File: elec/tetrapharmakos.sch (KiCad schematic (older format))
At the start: 12 parts

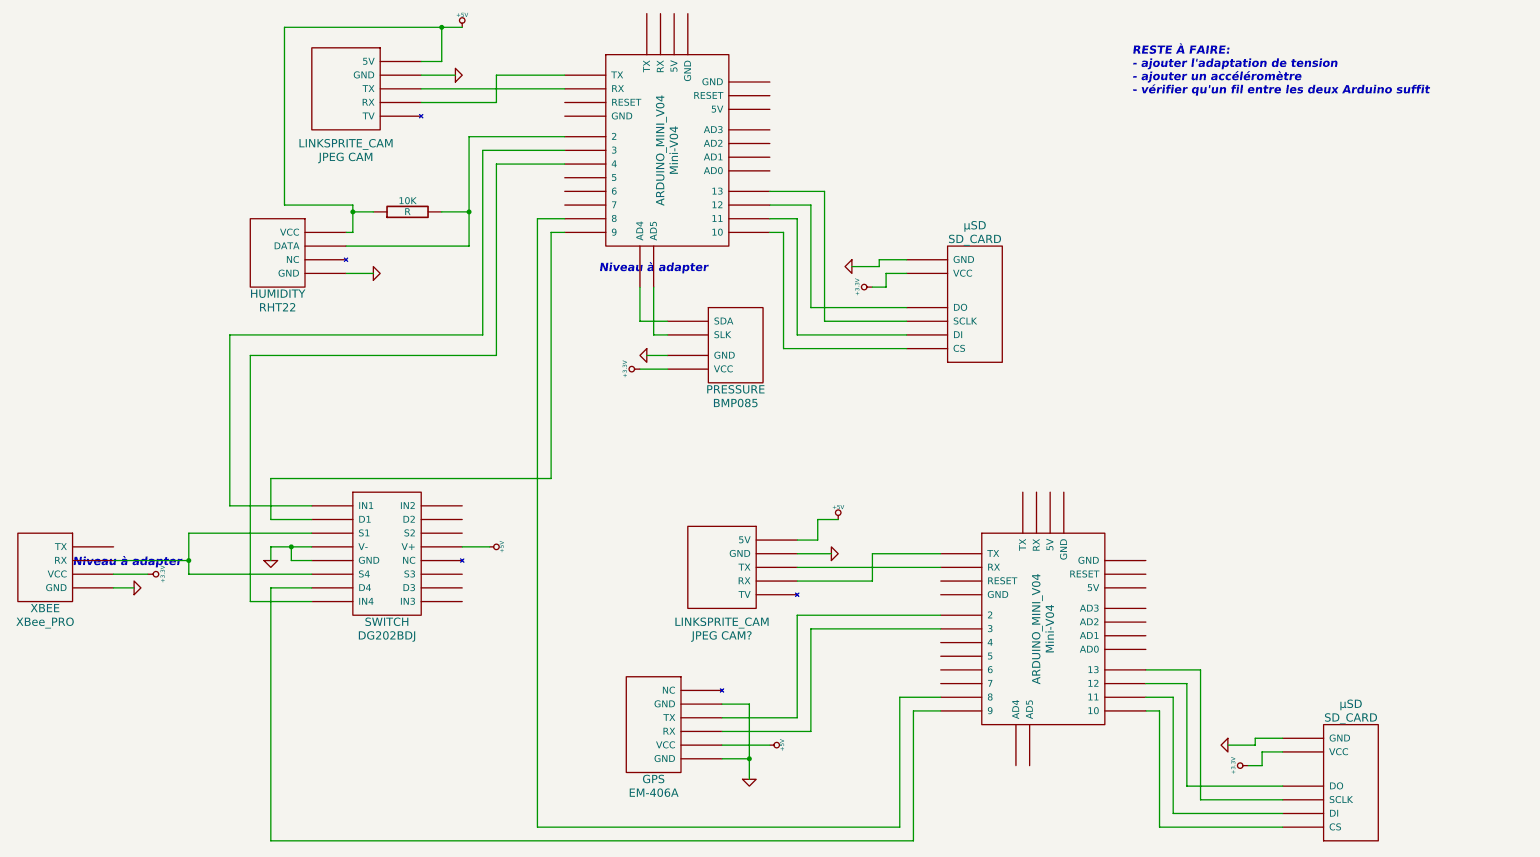
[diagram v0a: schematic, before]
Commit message: Ajout de l'accéléromètre numérique dans le schéma électronique
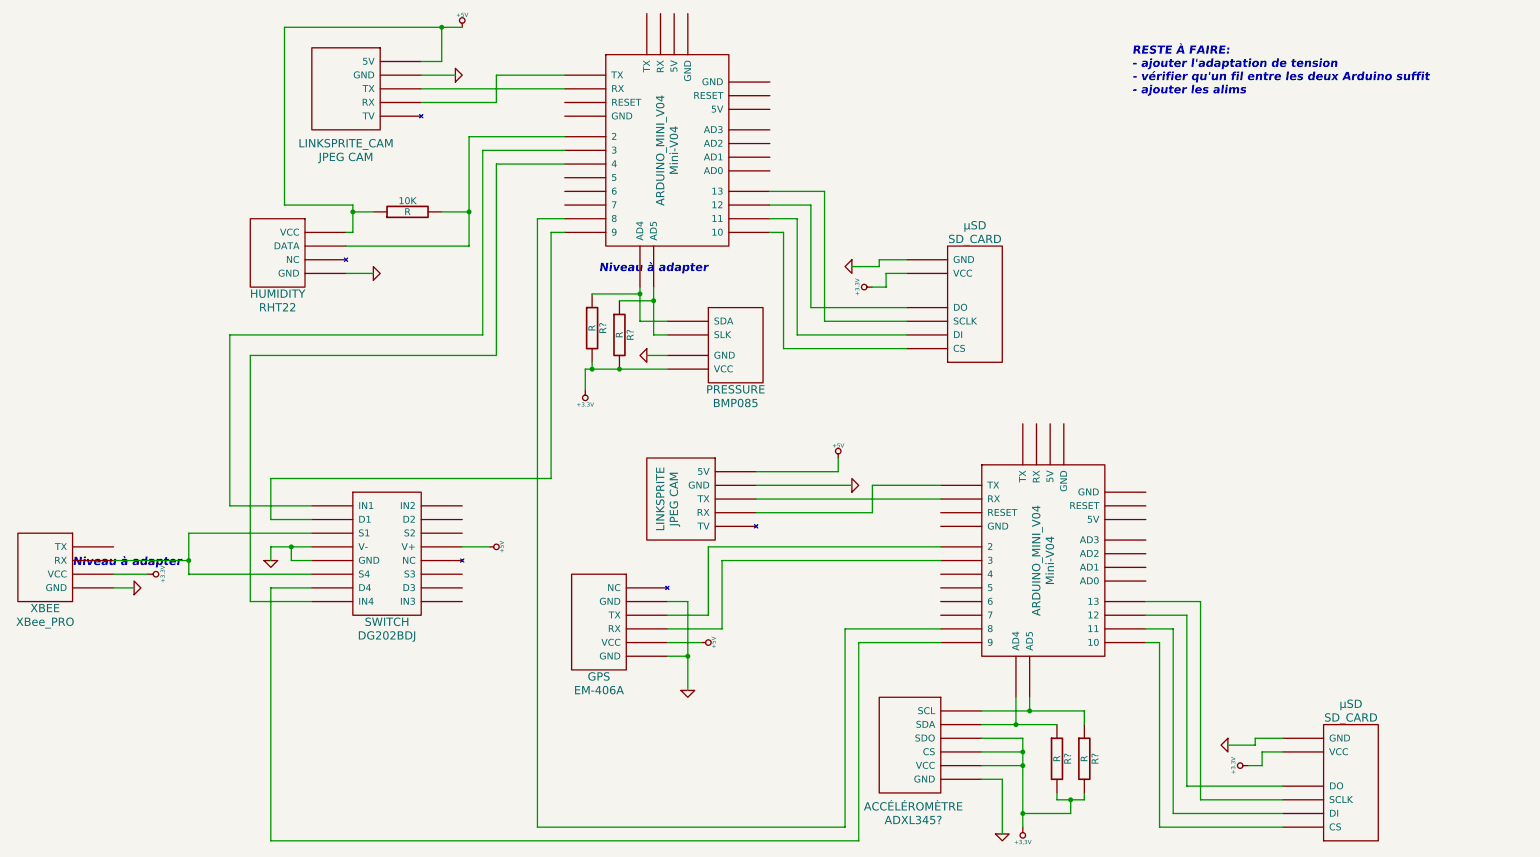
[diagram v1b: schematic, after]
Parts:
- added ADXL345?: ACCÉLÉROMÈTRE, symbol ACCÉLÉROMÈTRE
- added R? (x4): R, symbol R
- JPEG: renamed from JPEG~CAM?; value LINKSPRITE_CAM -> LINKSPRITE
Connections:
- net +3.3V: now also ADXL345?.~ (VCC), R?.2, R?.2, R?.2, R?.2
- net GND: now also ADXL345?.~ (VCC)
- net at Mini-V04.~ (TX): now also DG202BDJ.~ (V-)
- net at Mini-V04.~ (TX): now also ADXL345?.~ (VCC), R?.1; no longer Mini-V04.~ (TX)
- new net: Mini-V04.~ (TX), µSD.~ (VCC) (x8)
- new net: JPEG~CAM.~ (TX), Mini-V04.~ (TX) (x2)
- new net: BMP085.~ (VCC), Mini-V04.~ (TX), R?.1 (x2)
- new net: 10K.2, Mini-V04.~ (TX), RHT22.~ (VCC)
- new net: Mini-V04.~ (TX), Mini-V04.~ (TX)
- new net: DG202BDJ.~ (V-), Mini-V04.~ (TX) (x3)
- new net: JPEG.~ (TX), Mini-V04.~ (TX) (x2)
- new net: EM-406A.~ (VCC), Mini-V04.~ (TX) (x2)
- new net: ADXL345?.~ (VCC), Mini-V04.~ (TX), R?.1
- new net: DG202BDJ.~ (V-), XBee_PRO.~ (VCC)
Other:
- note added: "RESTE À FAIRE:\n- ajouter l'adaptation de tension\n- vérifier qu'un fil entre les deux Arduino suffit\n- ajouter les alims"
- note removed: "RESTE À FAIRE:\n- ajouter l'adaptation de tension\n- ajouter un accéléromètre\n- vérifier qu'un fil entre les deux Arduino suffit"
- moved on the sheet: EM-406A, JPEG CAM, Mini-V04

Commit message: changement des fichiers du programme de l'Arduino n°1 en liens symboliques
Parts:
- renumbered JPEG~CAM to JPEG
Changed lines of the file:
@@
-EESchema Schematic File Version 2  date dim. 29 juil. 2012 12:06:46 CEST
+EESchema Schematic File Version 2  date dim. 29 juil. 2012 13:25:51 CEST
 LIBS:tetrapharmakos
 LIBS:power
@@
 Comment4 ""
 $EndDescr
+Text Notes 7750 5900 0    60   Italic 12
+Niveau à adapter\n
 Wire Wire Line
 	4850 3550 4850 3700
@@
 74 7A 96 A9 4D 17 9A 8C 87 78 3F A7 08 11 BD 03 F1 CE 08 11 22 7A 07 22 EF 89 10 D1 3B 10 79 4F
 84 88 DE 81 C8 7B 22 44 F4 0E 44 DE 13 21 A2 77 20 F2 9E 08 11 BD 03 91 F7 44 88 E8 1D 88 BC 27
-42 44 EF E0 FF 01 E0 F9 98 82 53 18 56 10 00 00 00 00 49 45 4E 44 AE 42 60 82 00 $EndBitmap
+42 44 EF E0 FF 01 E0 F9 98 82 53 18 56 10 00 00 00 00 49 45 4E 44 AE 42 60 82 FF $EndBitmap
 EndData
 $EndBitmap
@@
 0B 91 BC 85 33 88 40 81 2D 61 06 57 74 FB 8A 75 19 34 52 0E 83 92 40 90 28 51 08 19 09 6B 19 90
 10 92 64 7D 75 6E 78 AF 96 F0 77 6E D9 BF DA E7 D2 5A 6B AD B5 D6 5A 6B AD B5 D6 5A 6B 7F EA 13
-62 30 5F E9 DA FC 67 7E 00 00 00 00 49 45 4E 44 AE 42 60 82 31 $EndBitmap
+62 30 5F E9 DA FC 67 7E 00 00 00 00 49 45 4E 44 AE 42 60 82 A9 $EndBitmap
 EndData
 $EndBitmap
@@
 	1    0    0    -1
 $EndComp
-Text Notes 1100 5000 0    60   Italic 12
+Text Notes 1350 5350 1    60   Italic 12
 Niveau à adapter\n
 Text Notes 4950 2850 0    60   Italic 12
@@
 $Comp
 L LINKSPRITE_CAM JPEG
-U 1 1 500BDE0A
+U 0 1 500BDE0A
 P 5550 4600
-F 0 "JPEG CAM" V 5500 4700 60  0000 C CNN
+F 0 "JPEG" V 5500 4700 60  0000 C CNN
 F 1 "LINKSPRITE" V 5400 4700 60  0000 C CNN
-	1    5550 4600
+	0    5550 4600
 	1    0    0    -1
 $EndComp
@@
 $EndComp
 $Comp
-L LINKSPRITE_CAM JPEG~CAM
-U 1 1 500AD02E
+L LINKSPRITE_CAM JPEG
+U 0 1 500AD02E
 P 3100 1600
 F 0 "JPEG CAM" H 3100 1200 60  0000 C CNN
 F 1 "LINKSPRITE_CAM" H 3100 1300 60  0000 C CNN
-	1    3100 1600
+	0    3100 1600
 	1    0    0    -1
 $EndComp

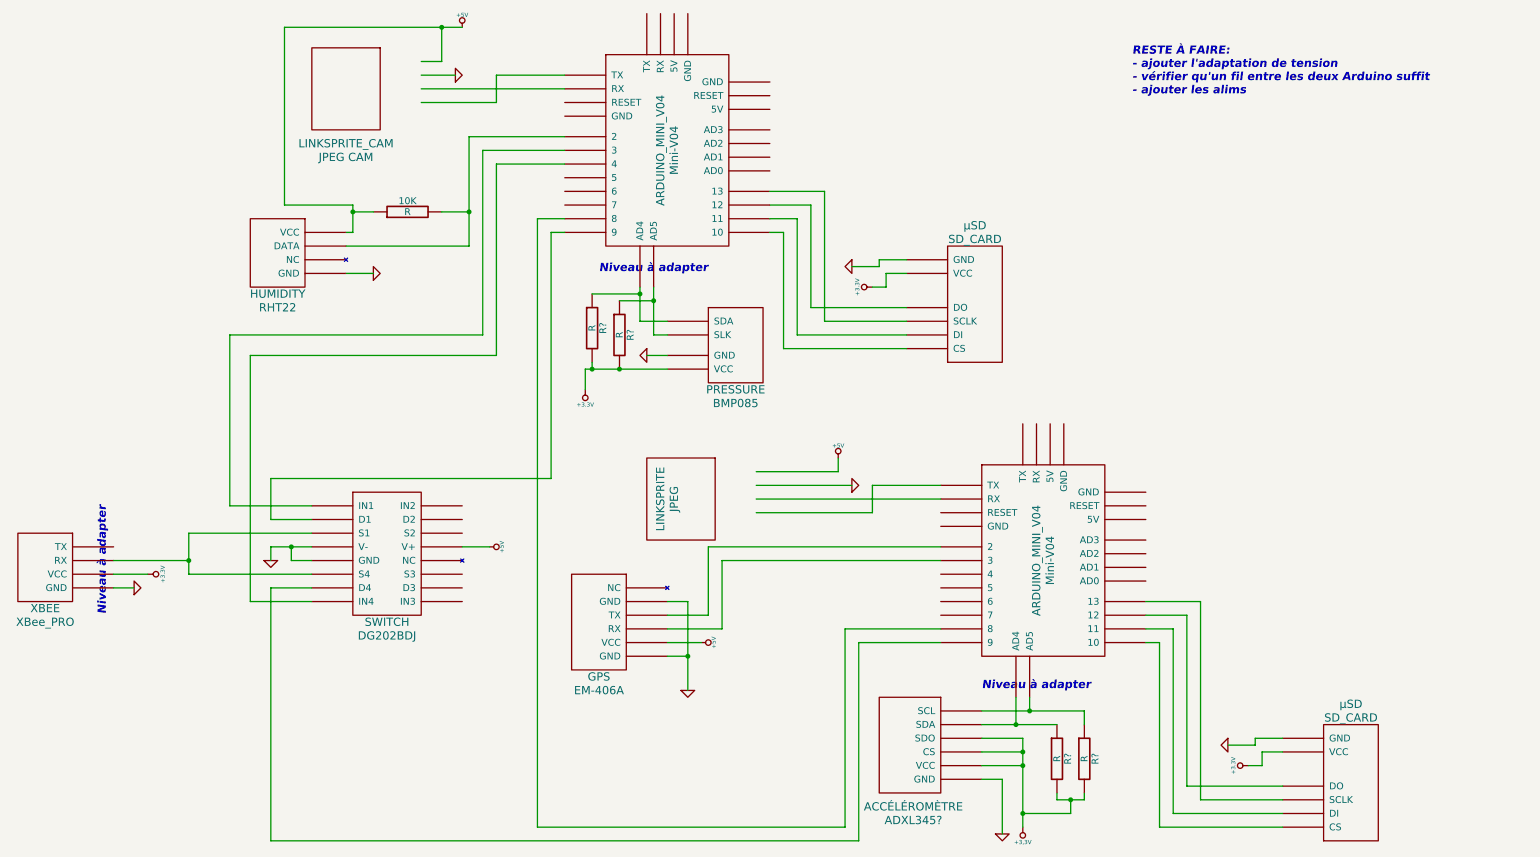
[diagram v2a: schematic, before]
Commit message: Suite du tuto jusqu'à la partie de la transmission de données sans-fil
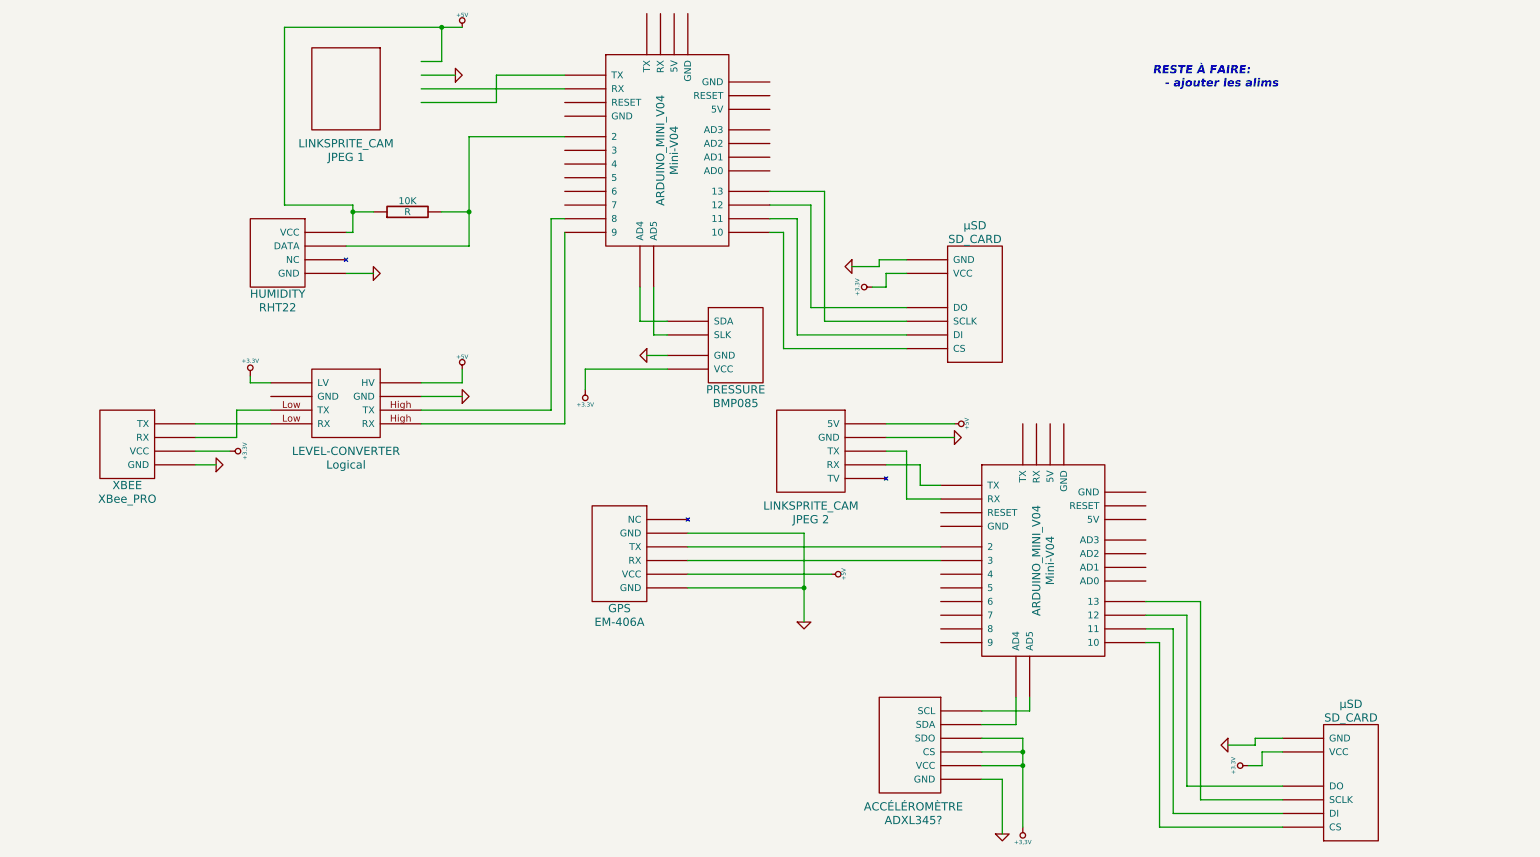
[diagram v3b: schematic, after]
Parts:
- removed DG202BDJ: SWITCH, symbol SWITCH
- removed JPEG: LINKSPRITE, symbol LINKSPRITE_CAM
- removed R? (x4): R, symbol R
- added unit 1 of JPEG
- added Logical: LEVEL-CONVERTER, symbol LEVEL-CONVERTER
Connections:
- wire segments 133 -> 101
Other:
- note added: "RESTE À FAIRE:\n - ajouter les alims"
- note removed: "Niveau à adapter\n"
- note removed: "RESTE À FAIRE:\n- ajouter l'adaptation de tension\n- vérifier qu'un fil entre les deux Arduino suffit\n- ajouter les alims"
- moved on the sheet: EM-406A, XBee_PRO
